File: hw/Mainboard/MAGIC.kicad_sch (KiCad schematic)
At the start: 15 parts, among them U18 SN74LVC4245APWR, U19 SN74LVC4245APWR, U20 SN74LVC4245APWR

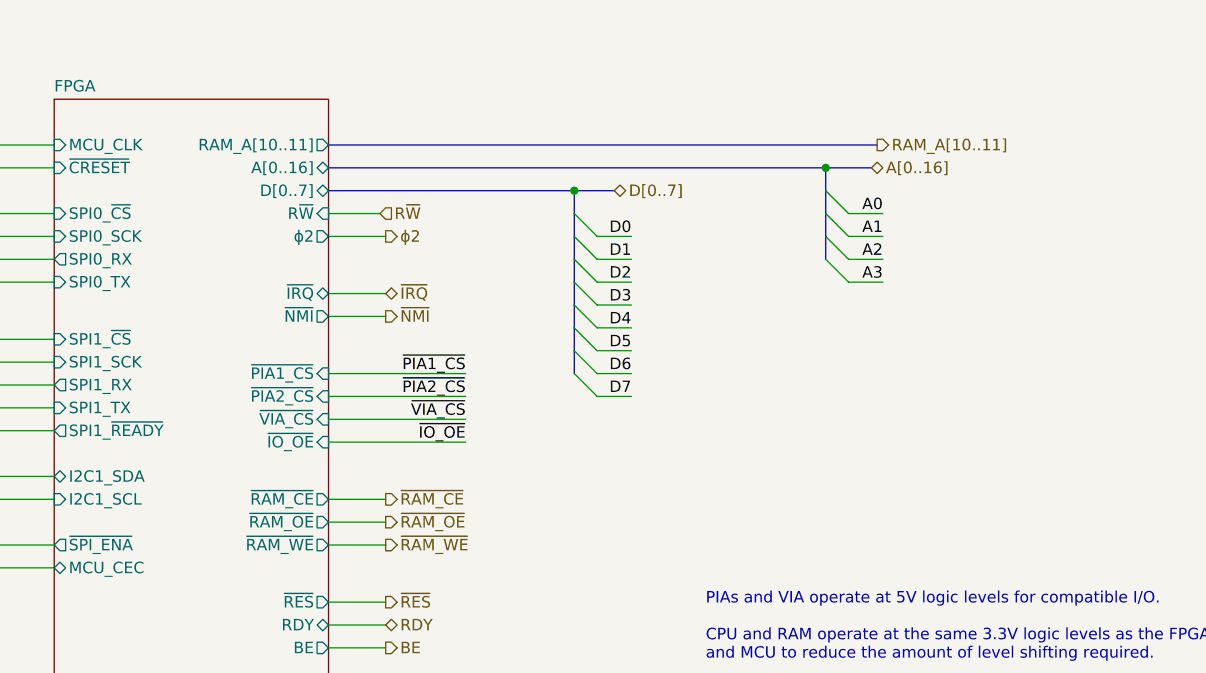
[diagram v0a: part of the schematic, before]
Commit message: hw: replace ram_ce with ram_a15
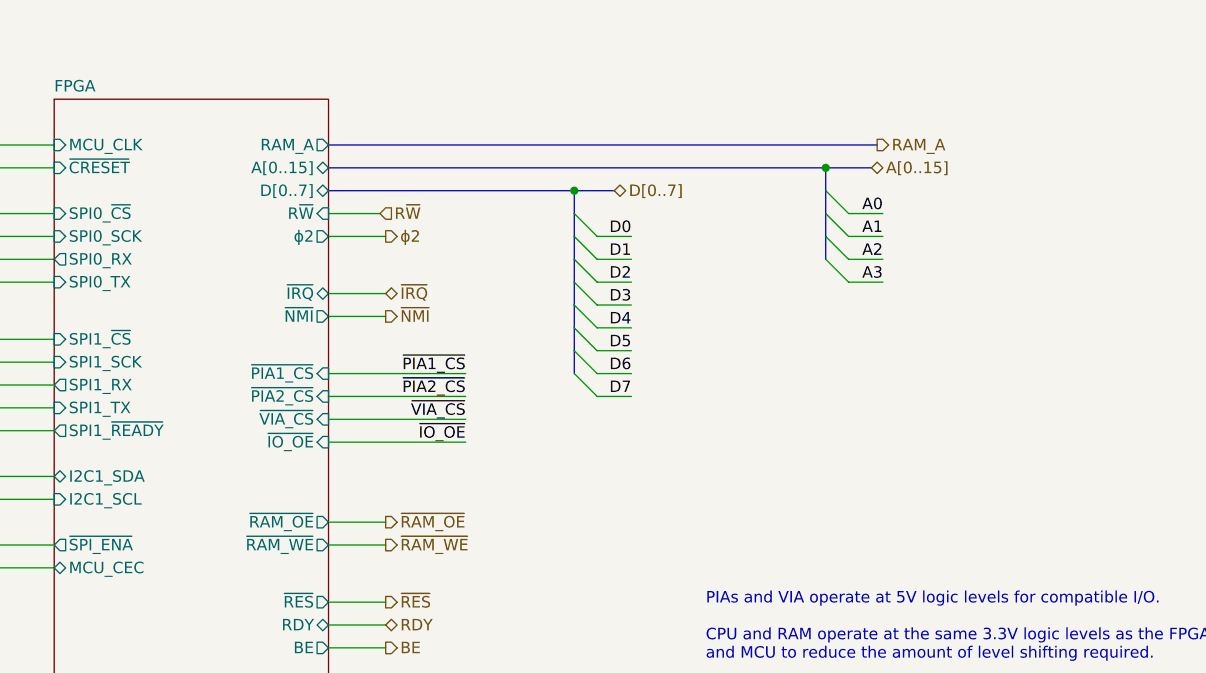
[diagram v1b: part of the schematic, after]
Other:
- sheet FPGA ports: added A[0..15], RAM_A; removed A[0..16], RAM_A[10..11], ~{RAM_CE}
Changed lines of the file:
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@@
-    (stroke (width 0) (type default) (color 0 0 0 0))
-  )
-  (wire (pts (xy 82.55 69.85) (xy 88.9 69.85))
     (stroke (width 0) (type default) (color 0 0 0 0))
   )
@@
     (effects (font (size 1.27 1.27)) (justify left))
   )
-  (hierarchical_label "RAM_A[10..11]" (shape output) (at 143.51 30.48 0)
+  (hierarchical_label "RAM_A" (shape output) (at 143.51 30.48 0)
     (effects (font (size 1.27 1.27)) (justify left))
   )
@@
     (effects (font (size 1.27 1.27)) (justify left))
   )
-  (hierarchical_label "A[0..16]" (shape bidirectional) (at 142.875 33.02 0)
+  (hierarchical_label "A[0..15]" (shape bidirectional) (at 142.875 33.02 0)
     (effects (font (size 1.27 1.27)) (justify left))
   )
   (hierarchical_label "GRAPHICS" (shape input) (at 107.315 118.11 0)
-    (effects (font (size 1.27 1.27)) (justify left))
-  )
-  (hierarchical_label "~{RAM_CE}" (shape output) (at 88.9 69.85 0)
     (effects (font (size 1.27 1.27)) (justify left))
   )
@@
       (effects (font (size 1.27 1.27)) (justify right))
     )
-    (pin "~{RAM_CE}" output (at 82.55 69.85 0)
-      (effects (font (size 1.27 1.27)) (justify right))
-    )
     (pin "~{RAM_WE}" output (at 82.55 74.93 0)
       (effects (font (size 1.27 1.27)) (justify right))
@@
       (effects (font (size 1.27 1.27)) (justify right))
     )
-    (pin "RAM_A[10..11]" output (at 82.55 30.48 0)
-      (effects (font (size 1.27 1.27)) (justify right))
-    )
-    (pin "A[0..16]" bidirectional (at 82.55 33.02 0)
-      (effects (font (size 1.27 1.27)) (justify right))
-    )
     (pin "SPI0_RX" output (at 52.07 43.18 180)
       (effects (font (size 1.27 1.27)) (justify left))
@@
       (effects (font (size 1.27 1.27)) (justify left))
     )
-  )
+    (pin "RAM_A" output (at 82.55 30.48 0)
+      (effects (font (size 1.27 1.27)) (justify right))
+    )
+    (pin "A[0..15]" bidirectional (at 82.55 33.02 0)
+      (effects (font (size 1.27 1.27)) (justify right))
+    )
+  )

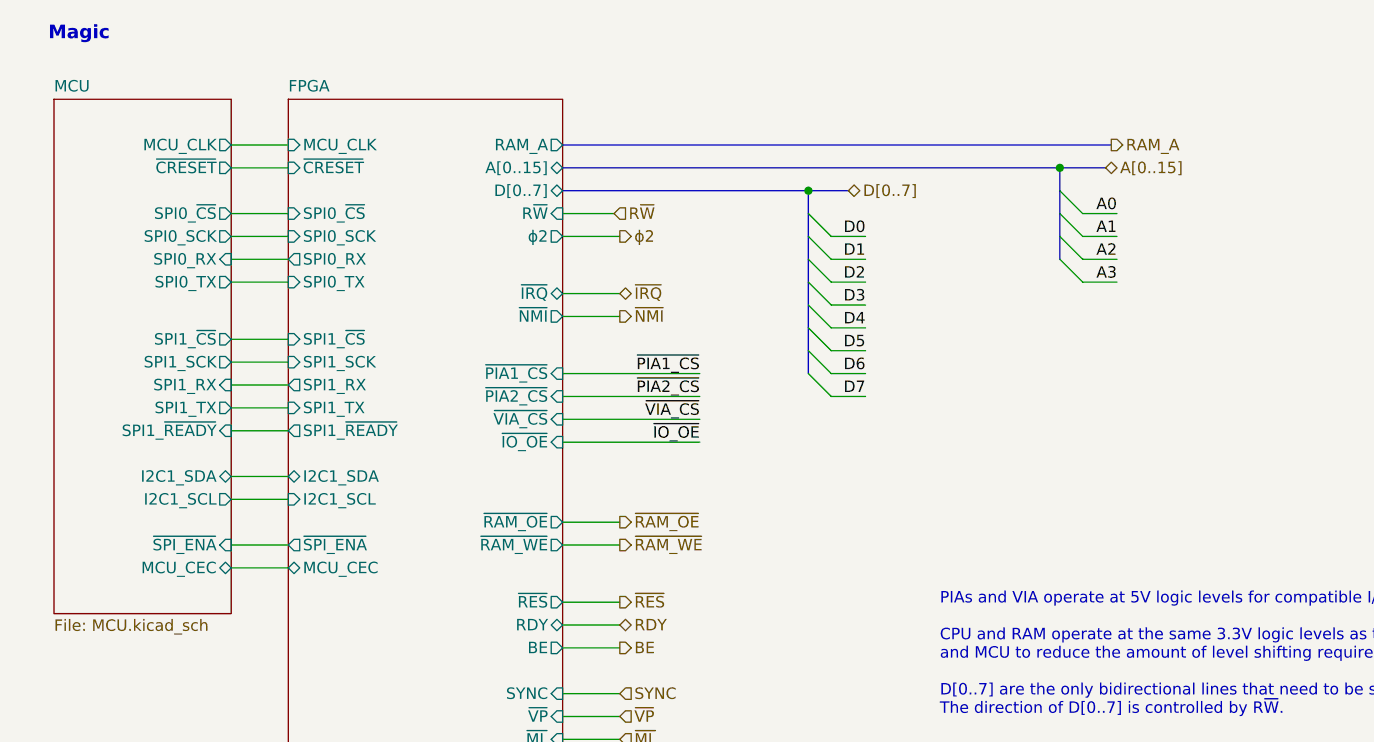
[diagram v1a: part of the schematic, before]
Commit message: hw: move DVI to separate hierarchical sheet, fix buses, annotate power
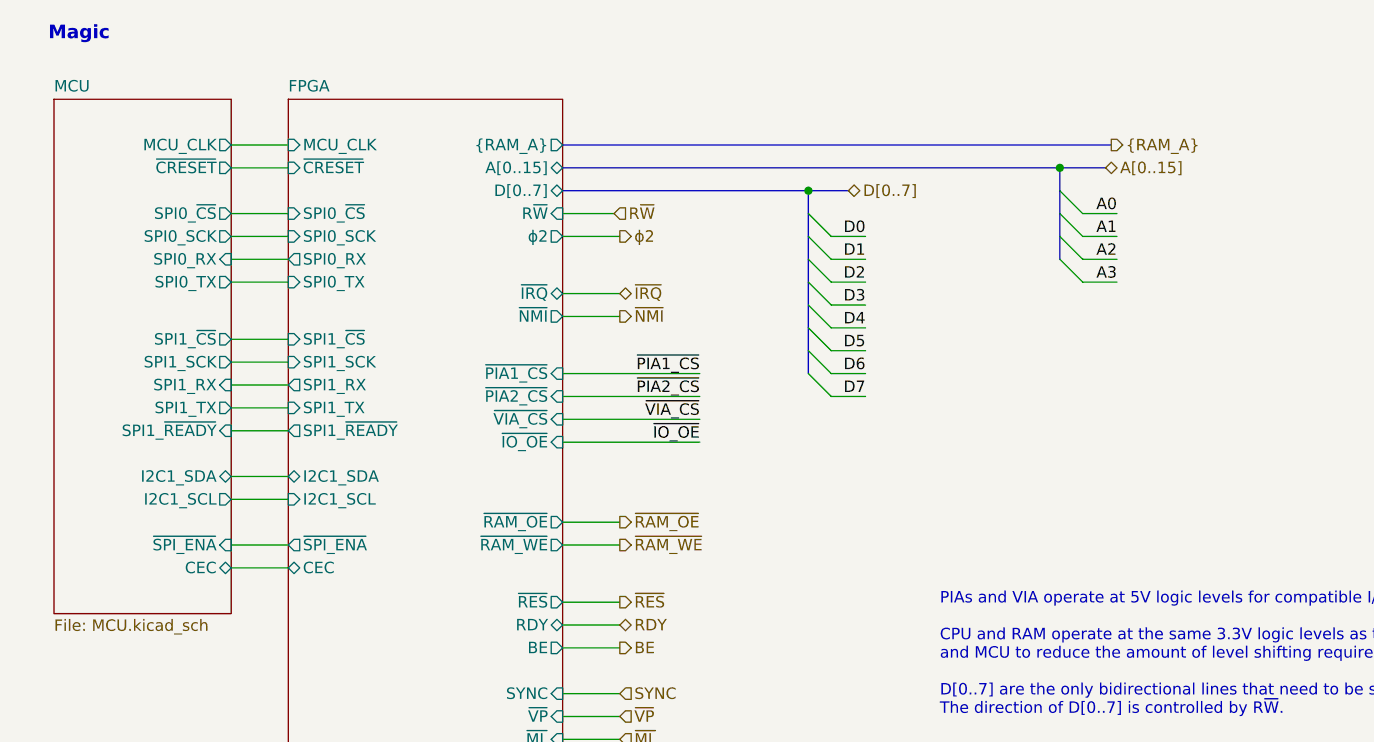
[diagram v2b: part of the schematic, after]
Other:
- sheet FPGA ports: added CEC, {RAM_A}; removed MCU_CEC, RAM_A
- sheet MCU ports: added CEC; removed MCU_CEC
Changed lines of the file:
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@@
     (effects (font (size 1.27 1.27)) (justify left))
   )
-  (hierarchical_label "RAM_A" (shape output) (at 143.51 30.48 0)
+  (hierarchical_label "{RAM_A}" (shape output) (at 143.51 30.48 0)
     (effects (font (size 1.27 1.27)) (justify left))
   )
@@
   (symbol (lib_id "power:GND") (at 25.4 191.77 0) (unit 1)
     (in_bom yes) (on_board yes)
-    (property "Reference" "#PWR?" (id 0) (at 25.4 198.12 0)
+    (property "Reference" "#PWR040" (id 0) (at 25.4 198.12 0)
       (effects (font (size 1.27 1.27)) hide)
     )
@@
   (symbol (lib_id "power:+5V") (at 25.4 180.34 0) (unit 1)
     (in_bom yes) (on_board yes) (fields_autoplaced)
-    (property "Reference" "#PWR?" (id 0) (at 25.4 184.15 0)
+    (property "Reference" "#PWR025" (id 0) (at 25.4 184.15 0)
       (effects (font (size 1.27 1.27)) hide)
     )
@@
   (symbol (lib_id "power:+5V") (at 227.33 127 0) (unit 1)
     (in_bom yes) (on_board yes) (fields_autoplaced)
-    (property "Reference" "#PWR?" (id 0) (at 227.33 130.81 0)
+    (property "Reference" "#PWR024" (id 0) (at 227.33 130.81 0)
       (effects (font (size 1.27 1.27)) hide)
     )
@@
   (symbol (lib_id "power:+5V") (at 226.06 24.13 0) (unit 1)
     (in_bom yes) (on_board yes) (fields_autoplaced)
-    (property "Reference" "#PWR?" (id 0) (at 226.06 27.94 0)
+    (property "Reference" "#PWR012" (id 0) (at 226.06 27.94 0)
       (effects (font (size 1.27 1.27)) hide)
     )
@@
   (symbol (lib_id "power:+5V") (at 226.06 76.2 0) (unit 1)
     (in_bom yes) (on_board yes) (fields_autoplaced)
-    (property "Reference" "#PWR?" (id 0) (at 226.06 80.01 0)
+    (property "Reference" "#PWR014" (id 0) (at 226.06 80.01 0)
       (effects (font (size 1.27 1.27)) hide)
     )
@@
   (symbol (lib_id "power:+3V3") (at 222.25 127 0) (mirror y) (unit 1)
     (in_bom yes) (on_board yes)
-    (property "Reference" "#PWR?" (id 0) (at 222.25 130.81 0)
+    (property "Reference" "#PWR022" (id 0) (at 222.25 130.81 0)
       (effects (font (size 1.27 1.27)) hide)
     )
@@
       (effects (font (size 1.27 1.27)) (justify left))
     )
-    (pin "MCU_CEC" bidirectional (at 52.07 77.47 180)
-      (effects (font (size 1.27 1.27)) (justify left))
-    )
-    (pin "RAM_A" output (at 82.55 30.48 0)
-      (effects (font (size 1.27 1.27)) (justify right))
+    (pin "CEC" bidirectional (at 52.07 77.47 180)
+      (effects (font (size 1.27 1.27)) (justify left))
     )
     (pin "A[0..15]" bidirectional (at 82.55 33.02 0)
+      (effects (font (size 1.27 1.27)) (justify right))
+    )
+    (pin "{RAM_A}" output (at 82.55 30.48 0)
       (effects (font (size 1.27 1.27)) (justify right))
     )
@@
       (effects (font (size 1.27 1.27)) (justify right))
     )
-    (pin "MCU_CEC" bidirectional (at 45.72 77.47 0)
-      (effects (font (size 1.27 1.27)) (justify right))
-    )
+    (pin "CEC" bidirectional (at 45.72 77.47 0)
+      (effects (font (size 1.27 1.27)) (justify right))
+    )

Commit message: hw: wip
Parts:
- added PT12, PT13: PowerTie_2, PET:NetTie-2_SMD_Pad_1.6_to_0.4mm, symbol PET:PowerTie_2
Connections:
- net +5V: now also PT12.1, PT13.1; no longer C18.1, C19.1, C20.1, U18.1 (VCCA), U19.1 (VCCA), U20.1 (VCCA)
- new net: C18.1, C20.1, PT12.2, U18.1 (VCCA), U19.1 (VCCA)
- new net: C19.1, PT13.2, U20.1 (VCCA)
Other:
- sheet FPGA ports: added FPGA_CLK, SWCLK, SWD, UART_RX, UART_TX; removed MCU_CLK
- sheet MCU ports: added FPGA_CLK, SWCLK, SWD, UART_RX, UART_TX; removed MCU_CLK
- moved on the sheet: C18, C19, C20, R52, R54, R55, R57, R58, R60, U18, U19, U20

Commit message: wip: support 8x16 keyboard matrix
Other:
- sheet FPGA ports: added I2C0_SCL, I2C0_SDA; removed none
- sheet MCU ports: added I2C0_SCL, I2C0_SDA; removed none
- moved on the sheet: C23, C27, C28

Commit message: hw: wip
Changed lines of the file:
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@@
     (stroke (width 0) (type default) (color 0 0 0 0))
   )
-  (wire (pts (xy 41.91 116.84) (xy 52.07 116.84))
+  (wire (pts (xy 45.72 116.84) (xy 52.07 116.84))
     (stroke (width 0) (type default) (color 0 0 0 0))
   )
@@
     (effects (font (size 1.27 1.27)) (justify left))
   )
-  (hierarchical_label "AUDIO" (shape output) (at 41.91 116.84 180)
+  (hierarchical_label "AUDIO" (shape output) (at 45.72 116.84 180)
     (effects (font (size 1.27 1.27)) (justify right))
   )
@@
     (pin "1")
   )
-  (sheet (at 52.07 25.4) (size 30.48 95.25) (fields_autoplaced)
+  (sheet (at 52.07 25.4) (size 30.48 99.06) (fields_autoplaced)
     (stroke (width 0) (type solid) (color 0 0 0 0))
     (fill (color 0 0 0 0.0000))
@@
       (effects (font (size 1.27 1.27)) (justify left bottom))
     )
-    (property "Sheet file" "FPGA.kicad_sch" (id 1) (at 52.07 121.2346 0)
+    (property "Sheet file" "FPGA.kicad_sch" (id 1) (at 52.07 125.0446 0)
       (effects (font (size 1.27 1.27)) (justify left top))
     )
@@
       (effects (font (size 1.27 1.27)) (justify right))
     )
+    (pin "VIA_CB2" input (at 82.55 110.49 0)
+      (effects (font (size 1.27 1.27)) (justify right))
+    )
+    (pin "DIAG" input (at 82.55 116.84 0)
+      (effects (font (size 1.27 1.27)) (justify right))
+    )
+    (pin "~{VP}" input (at 82.55 93.98 0)
+      (effects (font (size 1.27 1.27)) (justify right))
+    )
+    (pin "~{ML}" input (at 82.55 96.52 0)
+      (effects (font (size 1.27 1.27)) (justify right))
+    )
+    (pin "~{SO}" output (at 82.55 99.06 0)
+      (effects (font (size 1.27 1.27)) (justify right))
+    )
+    (pin "D[0..7]" bidirectional (at 82.55 35.56 0)
+      (effects (font (size 1.27 1.27)) (justify right))
+    )
+    (pin "SPI0_RX" output (at 52.07 43.18 180)
+      (effects (font (size 1.27 1.27)) (justify left))
+    )
+    (pin "SPI0_TX" input (at 52.07 45.72 180)
+      (effects (font (size 1.27 1.27)) (justify left))
+    )
+    (pin "SPI0_~{CS}" input (at 52.07 38.1 180)
+      (effects (font (size 1.27 1.27)) (justify left))
+    )
+    (pin "SPI1_RX" output (at 52.07 57.15 180)
+      (effects (font (size 1.27 1.27)) (justify left))
+    )
+    (pin "SPI1_~{CS}" input (at 52.07 52.07 180)
+      (effects (font (size 1.27 1.27)) (justify left))
+    )
+    (pin "SPI1_TX" input (at 52.07 59.69 180)
+      (effects (font (size 1.27 1.27)) (justify left))
+    )
+    (pin "SPI0_SCK" input (at 52.07 40.64 180)
+      (effects (font (size 1.27 1.27)) (justify left))
+    )
+    (pin "SPI1_~{READY}" output (at 52.07 62.23 180)
+      (effects (font (size 1.27 1.27)) (justify left))
+    )
+    (pin "SPI1_SCK" input (at 52.07 54.61 180)
+      (effects (font (size 1.27 1.27)) (justify left))
+    )
+    (pin "~{CRESET}" input (at 52.07 33.02 180)
+      (effects (font (size 1.27 1.27)) (justify left))
+    )
+    (pin "I2C1_SDA" bidirectional (at 52.07 74.93 180)
+      (effects (font (size 1.27 1.27)) (justify left))
+    )
+    (pin "I2C1_SCL" input (at 52.07 77.47 180)
+      (effects (font (size 1.27 1.27)) (justify left))
+    )
+    (pin "~{SPI_ENA}" output (at 52.07 82.55 180)
+      (effects (font (size 1.27 1.27)) (justify left))
+    )
+    (pin "CEC" bidirectional (at 52.07 85.09 180)
+      (effects (font (size 1.27 1.27)) (justify left))
+    )
+    (pin "A[0..15]" bidirectional (at 82.55 33.02 0)
+      (effects (font (size 1.27 1.27)) (justify right))
+    )
+    (pin "{RAM_A}" output (at 82.55 30.48 0)
+      (effects (font (size 1.27 1.27)) (justify right))
+    )
+    (pin "FPGA_CLK" input (at 52.07 30.48 180)
+      (effects (font (size 1.27 1.27)) (justify left))
+    )
+    (pin "SWD" bidirectional (at 52.07 92.71 180)
+      (effects (font (size 1.27 1.27)) (justify left))
+    )
+    (pin "SWCLK" input (at 52.07 90.17 180)
+      (effects (font (size 1.27 1.27)) (justify left))
+    )
+    (pin "UART_TX" input (at 52.07 95.25 180)
+      (effects (font (size 1.27 1.27)) (justify left))
+    )
+    (pin "UART_RX" output (at 52.07 97.79 180)
+      (effects (font (size 1.27 1.27)) (justify left))
+    )
+    (pin "I2C0_SCL" input (at 52.07 69.85 180)
+      (effects (font (size 1.27 1.27)) (justify left))
+    )
+    (pin "I2C0_SDA" bidirectional (at 52.07 67.31 180)
+      (effects (font (size 1.27 1.27)) (justify left))
+    )
     (pin "AUDIO" output (at 52.07 116.84 180)
       (effects (font (size 1.27 1.27)) (justify left))
     )
-    (pin "VIA_CB2" input (at 82.55 110.49 0)
-      (effects (font (size 1.27 1.27)) (justify right))
-    )
-    (pin "DIAG" input (at 82.55 116.84 0)
-      (effects (font (size 1.27 1.27)) (justify right))
-    )
-    (pin "~{VP}" input (at 82.55 93.98 0)
-      (effects (font (size 1.27 1.27)) (justify right))
-    )
-    (pin "~{ML}" input (at 82.55 96.52 0)
-      (effects (font (size 1.27 1.27)) (justify right))
-    )
-    (pin "~{SO}" output (at 82.55 99.06 0)
-      (effects (font (size 1.27 1.27)) (justify right))
-    )
-    (pin "D[0..7]" bidirectional (at 82.55 35.56 0)
-      (effects (font (size 1.27 1.27)) (justify right))
-    )
-    (pin "SPI0_RX" output (at 52.07 43.18 180)
-      (effects (font (size 1.27 1.27)) (justify left))
-    )
-    (pin "SPI0_TX" input (at 52.07 45.72 180)
-      (effects (font (size 1.27 1.27)) (justify left))
-    )
-    (pin "SPI0_~{CS}" input (at 52.07 38.1 180)
-      (effects (font (size 1.27 1.27)) (justify left))
-    )
-    (pin "SPI1_RX" output (at 52.07 57.15 180)
-      (effects (font (size 1.27 1.27)) (justify left))
-    )
-    (pin "SPI1_~{CS}" input (at 52.07 52.07 180)
-      (effects (font (size 1.27 1.27)) (justify left))
-    )
-    (pin "SPI1_TX" input (at 52.07 59.69 180)
-      (effects (font (size 1.27 1.27)) (justify left))
-    )
-    (pin "SPI0_SCK" input (at 52.07 40.64 180)
-      (effects (font (size 1.27 1.27)) (justify left))
-    )
-    (pin "SPI1_~{READY}" output (at 52.07 62.23 180)
-      (effects (font (size 1.27 1.27)) (justify left))
-    )
-    (pin "SPI1_SCK" input (at 52.07 54.61 180)
-      (effects (font (size 1.27 1.27)) (justify left))
-    )
-    (pin "~{CRESET}" input (at 52.07 33.02 180)
-      (effects (font (size 1.27 1.27)) (justify left))
-    )
-    (pin "I2C1_SDA" bidirectional (at 52.07 74.93 180)
-      (effects (font (size 1.27 1.27)) (justify left))
-    )
-    (pin "I2C1_SCL" input (at 52.07 77.47 180)
-      (effects (font (size 1.27 1.27)) (justify left))
-    )
-    (pin "~{SPI_ENA}" output (at 52.07 82.55 180)
-      (effects (font (size 1.27 1.27)) (justify left))
-    )
-    (pin "CEC" bidirectional (at 52.07 85.09 180)
-      (effects (font (size 1.27 1.27)) (justify left))
-    )
-    (pin "A[0..15]" bidirectional (at 82.55 33.02 0)
-      (effects (font (size 1.27 1.27)) (justify right))
-    )
-    (pin "{RAM_A}" output (at 82.55 30.48 0)
-      (effects (font (size 1.27 1.27)) (justify right))
-    )
-    (pin "FPGA_CLK" input (at 52.07 30.48 180)
-      (effects (font (size 1.27 1.27)) (justify left))
-    )
-    (pin "SWD" bidirectional (at 52.07 92.71 180)
-      (effects (font (size 1.27 1.27)) (justify left))
-    )
-    (pin "SWCLK" input (at 52.07 90.17 180)
-      (effects (font (size 1.27 1.27)) (justify left))
-    )
-    (pin "UART_TX" input (at 52.07 95.25 180)
-      (effects (font (size 1.27 1.27)) (justify left))
-    )
-    (pin "UART_RX" output (at 52.07 97.79 180)
-      (effects (font (size 1.27 1.27)) (justify left))
-    )
-    (pin "I2C0_SCL" input (at 52.07 69.85 180)
-      (effects (font (size 1.27 1.27)) (justify left))
-    )
-    (pin "I2C0_SDA" bidirectional (at 52.07 67.31 180)
-      (effects (font (size 1.27 1.27)) (justify left))
-    )
